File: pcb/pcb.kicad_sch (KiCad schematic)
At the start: 51 parts, among them J1 N!N, J2 Conn_01x02_Socket, J3 Conn_01x12_Socket, J4 Display_nice-view, J5 Conn_01x12_Socket, J6 Conn_01x12_Socket, J7 Conn_01x12_Socket, SW10 Switch, SW11 Switch, SW12 Switch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

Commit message: final pcb
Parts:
- added J8, J9: Conn_01x12_Socket, Connector_FFC-FPC:TE_1-84952-2_1x12-1MP_P1.0mm_Horizontal, symbol Connector:Conn_01x12_Socket
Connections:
- net +3.3V: now also J1.21 (3V3); no longer J1.27 (3V3)
- net BAT: now also J1.24 (BAT), J8.1 (Pin_1), J9.1 (Pin_1); no longer J1.30 (BAT)
- net CS: now also J1.1 (006)
- net GND: now also J1.23 (GND), J1.3 (GND), J8.2 (Pin_2), J9.2 (Pin_2); no longer J1.29 (GND), J1.5 (GND)
- net MOSI: no longer J1.2 (006)
- net RST: now also J1.22 (RST); no longer J1.28 (RST)
- net SCK: now also J1.5 (017); no longer J1.7 (020)
- net col0: now also J1.20 (031), S2.1 (A), J8.8 (Pin_8); no longer J1.26 (031)
- net col0_r: now also J1.12 (106), J9.8 (Pin_8); no longer J1.13 (106), S2.1 (A)
- net col1: now also J1.19 (029), S2.4 (B), J8.9 (Pin_9); no longer J1.25 (029)
- net col1_r: now also J1.11 (104), J9.9 (Pin_9); no longer J1.12 (104), S2.4 (B)
- net col2: now also J1.18 (002), S2.3 (C), J8.10 (Pin_10); no longer J1.24 (002)
- net col2_r: now also J1.10 (011), J9.10 (Pin_10); no longer J1.11 (011), S2.3 (C)
- net col3: now also J1.17 (115), S2.6 (D), J8.11 (Pin_11); no longer J1.23 (115)
- net col3_r: now also J1.9 (100), J9.11 (Pin_11); no longer J1.10 (100), S2.6 (D)
- net col4: now also J1.16 (113), S2.2 (CENTER), J8.12 (Pin_12); no longer J1.22 (113)
- net col4_r: now also J1.8 (024), J9.12 (Pin_12); no longer J1.9 (024), S2.2 (CENTER)
- net row0: now also J1.15 (111), J8.3 (Pin_3), J9.3 (Pin_3); no longer J1.21 (111)
- net row1: now also J1.14 (010), J8.4 (Pin_4), J9.4 (Pin_4); no longer J1.20 (010)
- net row2: now also J1.13 (009), J8.5 (Pin_5), J9.5 (Pin_5); no longer J1.19 (009)
- net row3: now also J1.7 (022), J8.6 (Pin_6), J9.6 (Pin_6); no longer J1.8 (022)
- net row4: now also J1.2 (008), J8.7 (Pin_7), J9.7 (Pin_7); no longer J1.3 (008)
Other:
- moved on the sheet: J2, J3, J4, J5, J6, J7, SW21, SW22

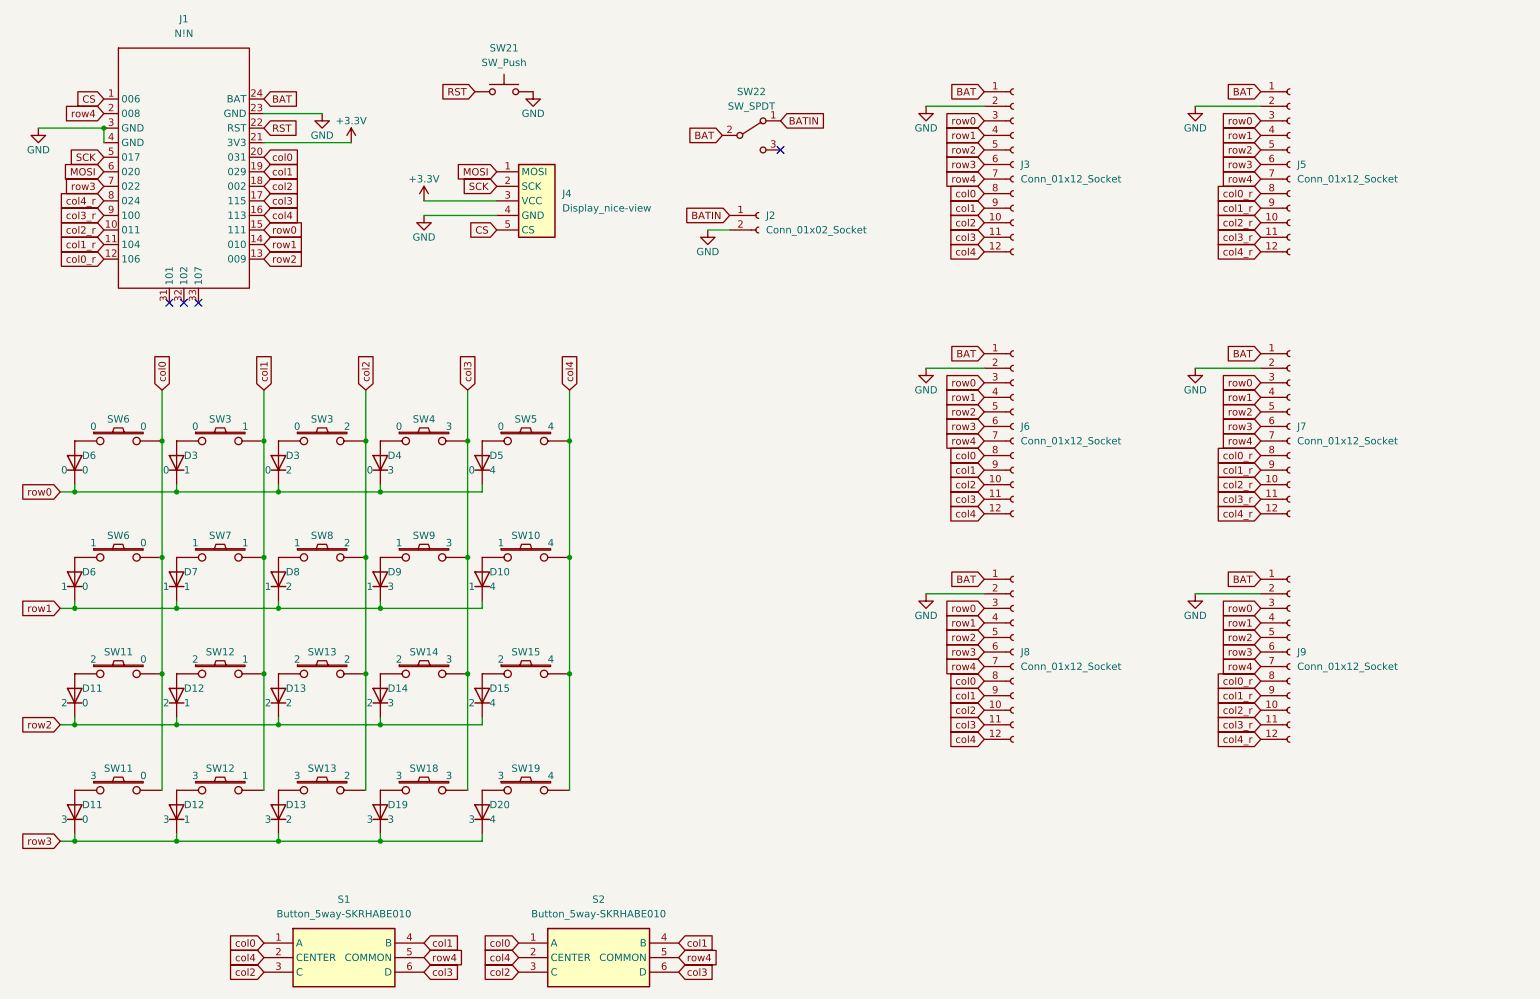
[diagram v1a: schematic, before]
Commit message: improve niceview pin mappings
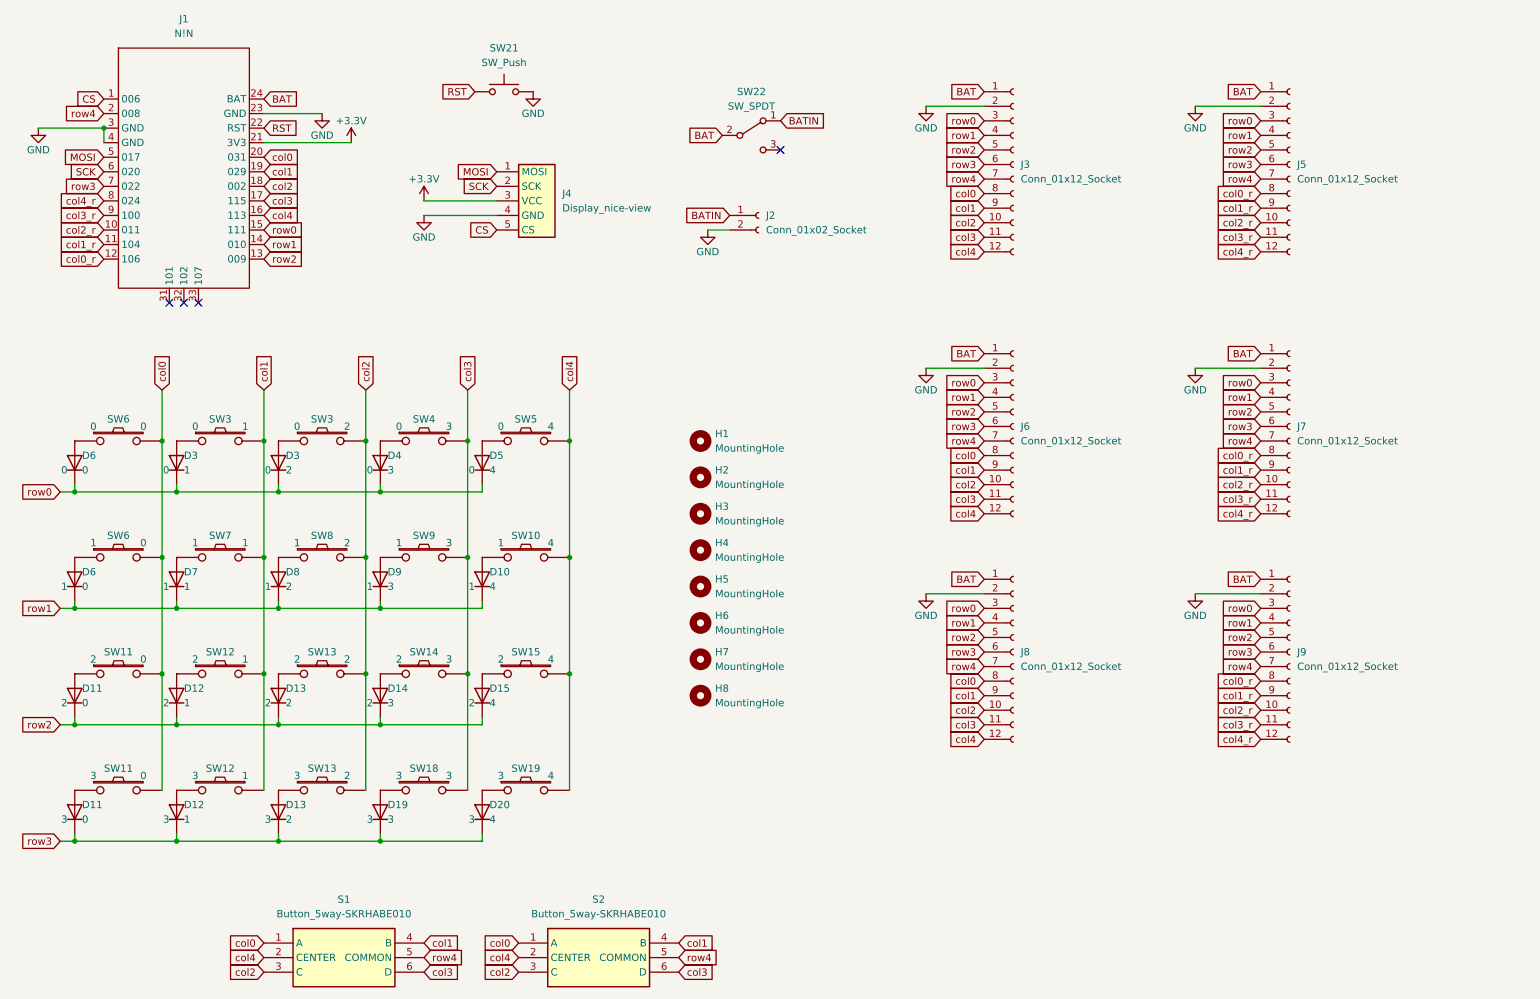
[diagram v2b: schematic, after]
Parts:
- added H1, H2, H3, H4, H5, H6, H7, H8: MountingHole, zzkeeb:Hole_M2-TH, symbol Mechanical:MountingHole
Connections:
- net MOSI: now also J1.5 (017); no longer J1.6 (020)
- net SCK: now also J1.6 (020); no longer J1.5 (017)
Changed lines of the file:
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@@
+    )
+  )
+  (global_label "MOSI" (shape input) (at 35.56 43.18 180) (fields_autoplaced)
+    (effects (font (size 1.27 1.27)) (justify right))
+    (property "Intersheetrefs" "${INTERSHEET_REFS}" (at 27.9786 43.18 0)
+      (effects (font (size 1.27 1.27)) (justify right) hide)
     )
   )
@@
     )
   )
+  (global_label "SCK" (shape input) (at 35.56 45.72 180) (fields_autoplaced)
+    (effects (font (size 1.27 1.27)) (justify right))
+    (property "Intersheetrefs" "${INTERSHEET_REFS}" (at 28.8253 45.72 0)
+      (effects (font (size 1.27 1.27)) (justify right) hide)
+    )
+  )
   (global_label "col0" (shape input) (at 189.23 49.53 180) (fields_autoplaced)
     (effects (font (size 1.27 1.27)) (justify right))
@@
     )
   )
-  (global_label "SCK" (shape input) (at 35.56 43.18 180) (fields_autoplaced)
-    (effects (font (size 1.27 1.27)) (justify right))
-    (property "Intersheetrefs" "${INTERSHEET_REFS}" (at 28.8253 43.18 0)
-      (effects (font (size 1.27 1.27)) (justify right) hide)
-    )
-  )
   (global_label "RST" (shape input) (at 100.33 31.75 180) (fields_autoplaced)
     (effects (font (size 1.27 1.27)) (justify right))
@@
     )
   )
-  (global_label "MOSI" (shape input) (at 35.56 45.72 180) (fields_autoplaced)
-    (effects (font (size 1.27 1.27)) (justify right))
-    (property "Intersheetrefs" "${INTERSHEET_REFS}" (at 27.9786 45.72 0)
-      (effects (font (size 1.27 1.27)) (justify right) hide)
-    )
-  )
   (global_label "col3" (shape input) (at 63.5 50.8 0) (fields_autoplaced)
     (effects (font (size 1.27 1.27)) (justify left))
@@
         (path "/ebd24df5-909b-47ae-ba78-ebcdd375bb76"
           (reference "D8") (unit 1)
+        )
+      )
+    )
+  )
+  (symbol (lib_id "Mechanical:MountingHole") (at 139.7 124.46 0) (unit 1)
+    (in_bom yes) (on_board yes) (dnp no) (fields_autoplaced)
+    (property "Reference" "H6" (at 142.24 123.19 0)
+      (effects (font (size 1.27 1.27)) (justify left))
+    )
+    (property "Value" "MountingHole" (at 142.24 125.73 0)
+      (effects (font (size 1.27 1.27)) (justify left))
+    )
+    (property "Footprint" "zzkeeb:Hole_M2-TH" (at 139.7 124.46 0)
+      (effects (font (size 1.27 1.27)) hide)
+    )
+    (property "Datasheet" "~" (at 139.7 124.46 0)
+      (effects (font (size 1.27 1.27)) hide)
+    )
+    (instances
+      (project "pcb"
+        (path "/ebd24df5-909b-47ae-ba78-ebcdd375bb76"
+          (reference "H6") (unit 1)
+        )
+      )
+    )
+  )
+  (symbol (lib_id "Mechanical:MountingHole") (at 139.7 92.71 0) (unit 1)
+    (in_bom yes) (on_board yes) (dnp no) (fields_autoplaced)
+    (property "Reference" "H1" (at 142.24 91.44 0)
+      (effects (font (size 1.27 1.27)) (justify left))
+    )
+    (property "Value" "MountingHole" (at 142.24 93.98 0)
+      (effects (font (size 1.27 1.27)) (justify left))
+    )
+    (property "Footprint" "zzkeeb:Hole_M2-TH" (at 139.7 92.71 0)
+      (effects (font (size 1.27 1.27)) hide)
+    )
+    (property "Datasheet" "~" (at 139.7 92.71 0)
+      (effects (font (size 1.27 1.27)) hide)
+    )
+    (instances
+      (project "pcb"
+        (path "/ebd24df5-909b-47ae-ba78-ebcdd375bb76"
+          (reference "H1") (unit 1)
         )
       )
@@
     )
   )
+  (symbol (lib_id "Mechanical:MountingHole") (at 139.7 99.06 0) (unit 1)
+    (in_bom yes) (on_board yes) (dnp no) (fields_autoplaced)
+    (property "Reference" "H2" (at 142.24 97.79 0)
+      (effects (font (size 1.27 1.27)) (justify left))
+    )
+    (property "Value" "MountingHole" (at 142.24 100.33 0)
+      (effects (font (size 1.27 1.27)) (justify left))
+    )
+    (property "Footprint" "zzkeeb:Hole_M2-TH" (at 139.7 99.06 0)
+      (effects (font (size 1.27 1.27)) hide)
+    )
+    (property "Datasheet" "~" (at 139.7 99.06 0)
+      (effects (font (size 1.27 1.27)) hide)
+    )
+    (instances
+      (project "pcb"
+        (path "/ebd24df5-909b-47ae-ba78-ebcdd375bb76"
+          (reference "H2") (unit 1)
+        )
+      )
+    )
+  )
   (symbol (lib_id "zzkeeb:Diode") (at 83.82 96.52 0) (unit 1)
     (in_bom yes) (on_board yes) (dnp no) (fields_autoplaced)
@@
         (path "/ebd24df5-909b-47ae-ba78-ebcdd375bb76"
           (reference "D19") (unit 1)
+        )
+      )
+    )
+  )
+  (symbol (lib_id "Mechanical:MountingHole") (at 139.7 118.11 0) (unit 1)
+    (in_bom yes) (on_board yes) (dnp no) (fields_autoplaced)
+    (property "Reference" "H5" (at 142.24 116.84 0)
+      (effects (font (size 1.27 1.27)) (justify left))
+    )
+    (property "Value" "MountingHole" (at 142.24 119.38 0)
+      (effects (font (size 1.27 1.27)) (justify left))
+    )
+    (property "Footprint" "zzkeeb:Hole_M2-TH" (at 139.7 118.11 0)
+      (effects (font (size 1.27 1.27)) hide)
+    )
+    (property "Datasheet" "~" (at 139.7 118.11 0)
+      (effects (font (size 1.27 1.27)) hide)
+    )
+    (instances
+      (project "pcb"
+        (path "/ebd24df5-909b-47ae-ba78-ebcdd375bb76"
+          (reference "H5") (unit 1)
         )
       )
@@
     )
   )
+  (symbol (lib_id "Mechanical:MountingHole") (at 139.7 105.41 0) (unit 1)
+    (in_bom yes) (on_board yes) (dnp no) (fields_autoplaced)
+    (property "Reference" "H3" (at 142.24 104.14 0)
+      (effects (font (size 1.27 1.27)) (justify left))
+    )
+    (property "Value" "MountingHole" (at 142.24 106.68 0)
+      (effects (font (size 1.27 1.27)) (justify left))
+    )
+    (property "Footprint" "zzkeeb:Hole_M2-TH" (at 139.7 105.41 0)
+      (effects (font (size 1.27 1.27)) hide)
+    )
+    (property "Datasheet" "~" (at 139.7 105.41 0)
+      (effects (font (size 1.27 1.27)) hide)
+    )
+    (instances
+      (project "pcb"
+        (path "/ebd24df5-909b-47ae-ba78-ebcdd375bb76"
+          (reference "H3") (unit 1)
+        )
+      )
+    )
+  )
   (symbol (lib_id "power:GND") (at 73.66 35.56 0) (unit 1)
     (in_bom yes) (on_board yes) (dnp no)
@@
     )
   )
+  (symbol (lib_id "Mechanical:MountingHole") (at 139.7 111.76 0) (unit 1)
+    (in_bom yes) (on_board yes) (dnp no) (fields_autoplaced)
+    (property "Reference" "H4" (at 142.24 110.49 0)
+      (effects (font (size 1.27 1.27)) (justify left))
+    )
+    (property "Value" "MountingHole" (at 142.24 113.03 0)
+      (effects (font (size 1.27 1.27)) (justify left))
+    )
+    (property "Footprint" "zzkeeb:Hole_M2-TH" (at 139.7 111.76 0)
+      (effects (font (size 1.27 1.27)) hide)
+    )
+    (property "Datasheet" "~" (at 139.7 111.76 0)
+      (effects (font (size 1.27 1.27)) hide)
+    )
+    (instances
+      (project "pcb"
+        (path "/ebd24df5-909b-47ae-ba78-ebcdd375bb76"
+          (reference "H4") (unit 1)
+        )
+      )
+    )
+  )
   (symbol (lib_id "power:GND") (at 179.07 119.38 0) (unit 1)
     (in_bom yes) (on_board yes) (dnp no)
@@
         )
       )
+    )
+  )
+  (symbol (lib_id "Mechanical:MountingHole") (at 139.7 130.81 0) (unit 1)
+    (in_bom yes) (on_board yes) (dnp no) (fields_autoplaced)
+    (property "Reference" "H7" (at 142.24 129.54 0)
+      (effects (font (size 1.27 1.27)) (justify left))
+    )
+    (property "Value" "MountingHole" (at 142.24 132.08 0)
+      (effects (font (size 1.27 1.27)) (justify left))
+    )
+    (property "Footprint" "zzkeeb:Hole_M2-TH" (at 139.7 130.81 0)
+      (effects (font (size 1.27 1.27)) hide)
+    )
+    (property "Datasheet" "~" (at 139.7 130.81 0)
+      (effects (font (size 1.27 1.27)) hide)
+    )
+    (instances
+      (project "pcb"
+        (path "/ebd24df5-909b-47ae-ba78-ebcdd375bb76"
+          (reference "H7") (unit 1)
+        )
+      )
+    )
+  )
+  (symbol (lib_id "Mechanical:MountingHole") (at 139.7 137.16 0) (unit 1)
+    (in_bom yes) (on_board yes) (dnp no) (fields_autoplaced)
+    (property "Reference" "H8" (at 142.24 135.89 0)
+      (effects (font (size 1.27 1.27)) (justify left))
+    )
+    (property "Value" "MountingHole" (at 142.24 138.43 0)
+      (effects (font (size 1.27 1.27)) (justify left))
+    )
+    (property "Footprint" "zzkeeb:Hole_M2-TH" (at 139.7 137.16 0)
+      (effects (font (size 1.27 1.27)) hide)
+    )
+    (property "Datasheet" "~" (at 139.7 137.16 0)
+      (effects (font (size 1.27 1.27)) hide)
+    )
+    (instances
+      (project "pcb"
+        (path "/ebd24df5-909b-47ae-ba78-ebcdd375bb76"
+          (reference "H8") (unit 1)
+        )
+      )

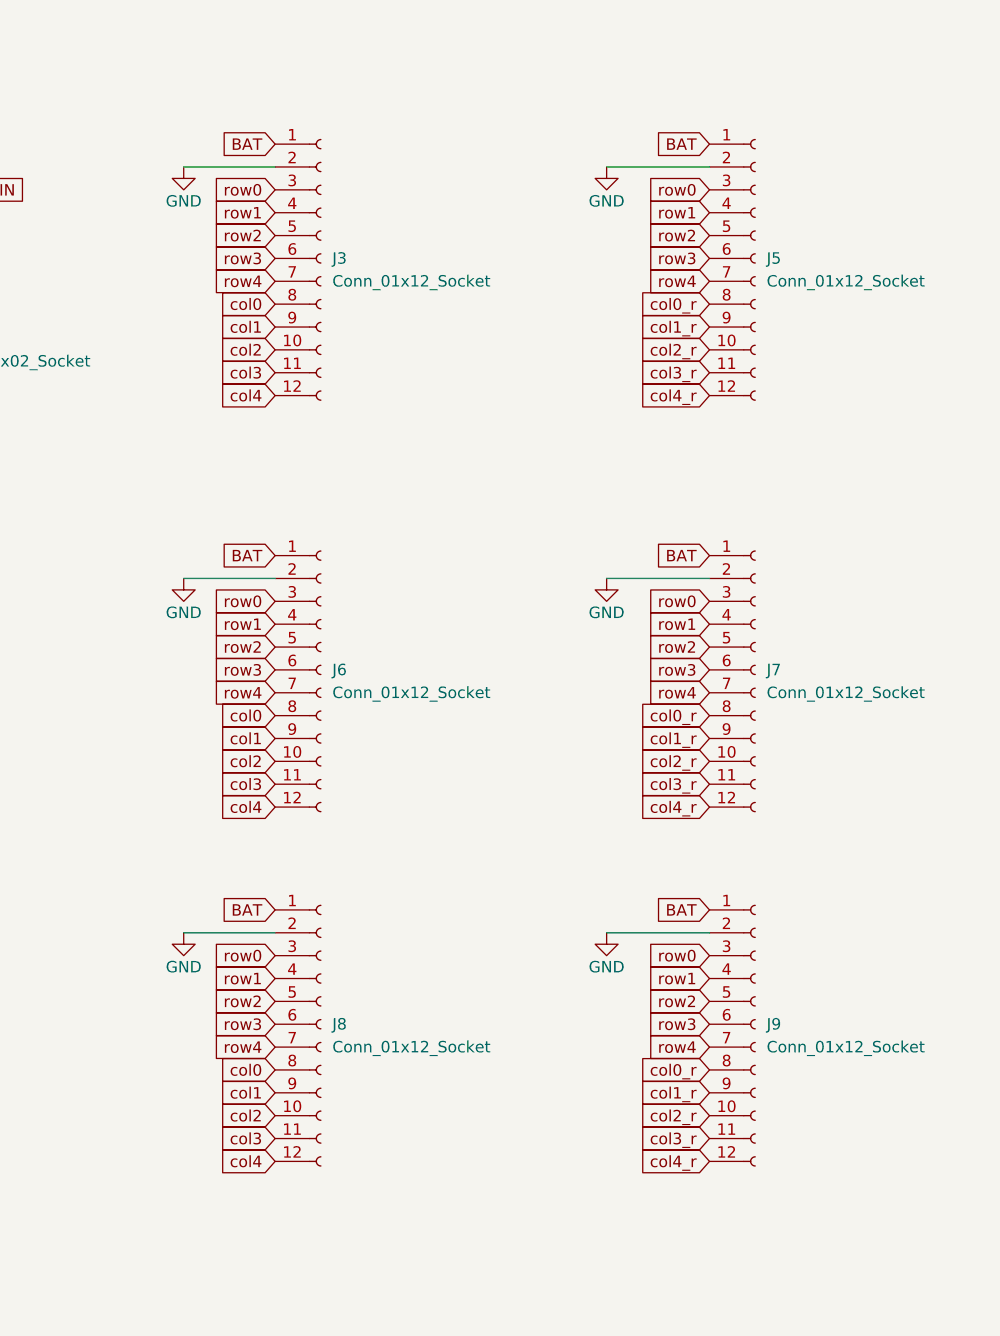
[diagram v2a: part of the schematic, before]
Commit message: simplify pcb, reduce cover size
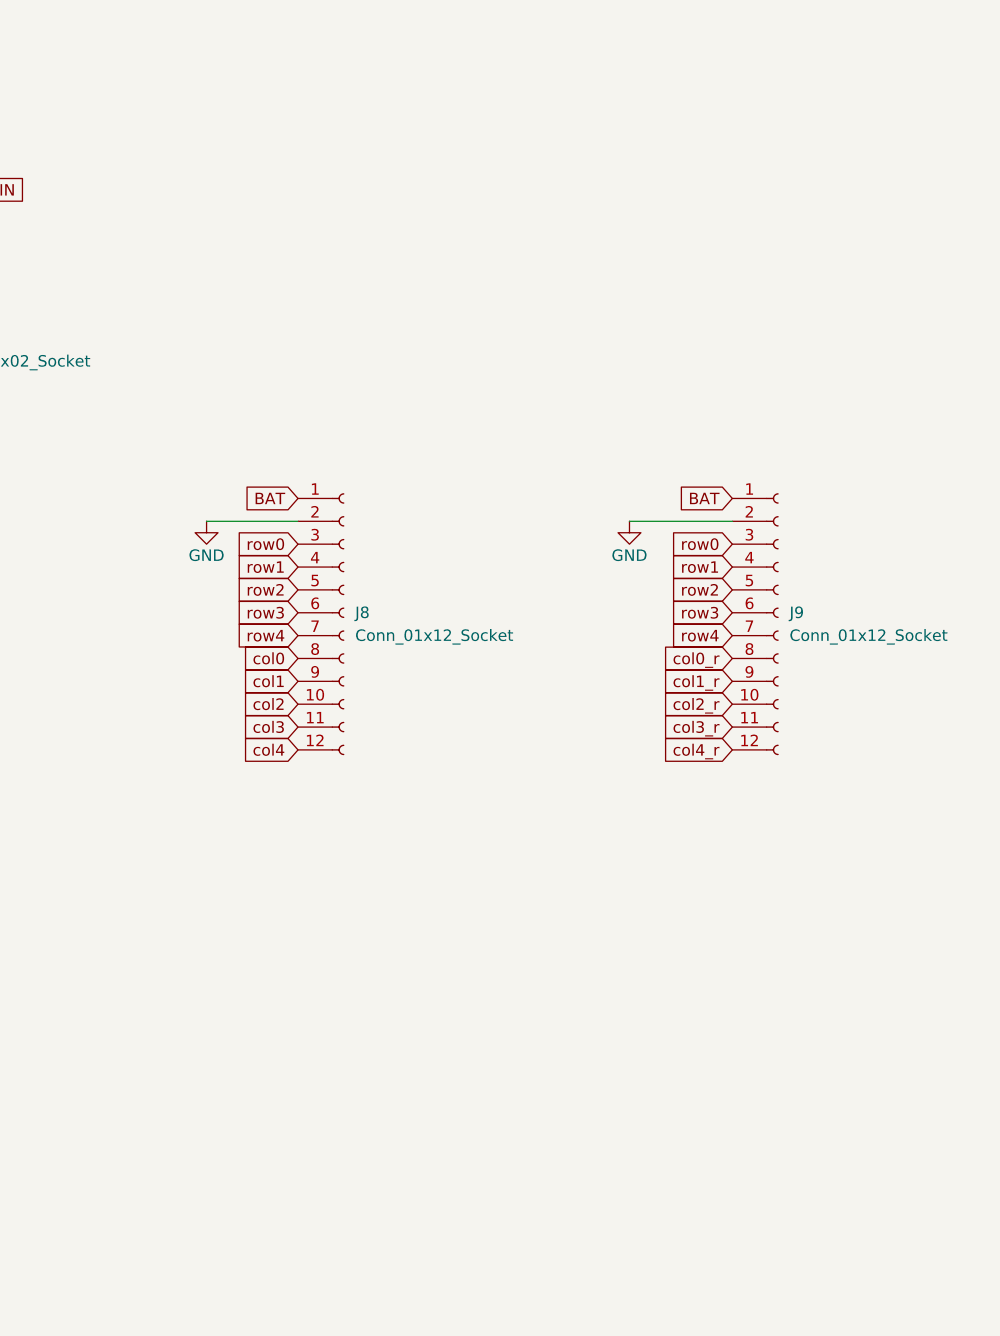
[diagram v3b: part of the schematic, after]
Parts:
- removed J3, J5: Conn_01x12_Socket, zzkeeb:Connector_JST-1x12-P1.25mm, symbol Connector:Conn_01x12_Socket
- removed J6, J7: Conn_01x12_Socket, zzkeeb:Connector_VIK-horizontal-keyboard, symbol Connector:Conn_01x12_Socket
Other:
- moved on the sheet: J8, J9
